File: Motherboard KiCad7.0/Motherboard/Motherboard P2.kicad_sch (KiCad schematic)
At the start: 33 parts, among them J3 2-1445057-2, J4 2-1445057-2, J5 2-1445057-2, J6 2-1445057-2, J7 2-1445057-2, Q1 AO3400A, Q2 AO3400A, Q3 AO3400A, Q4 AO3400A, Q5 AO3400A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

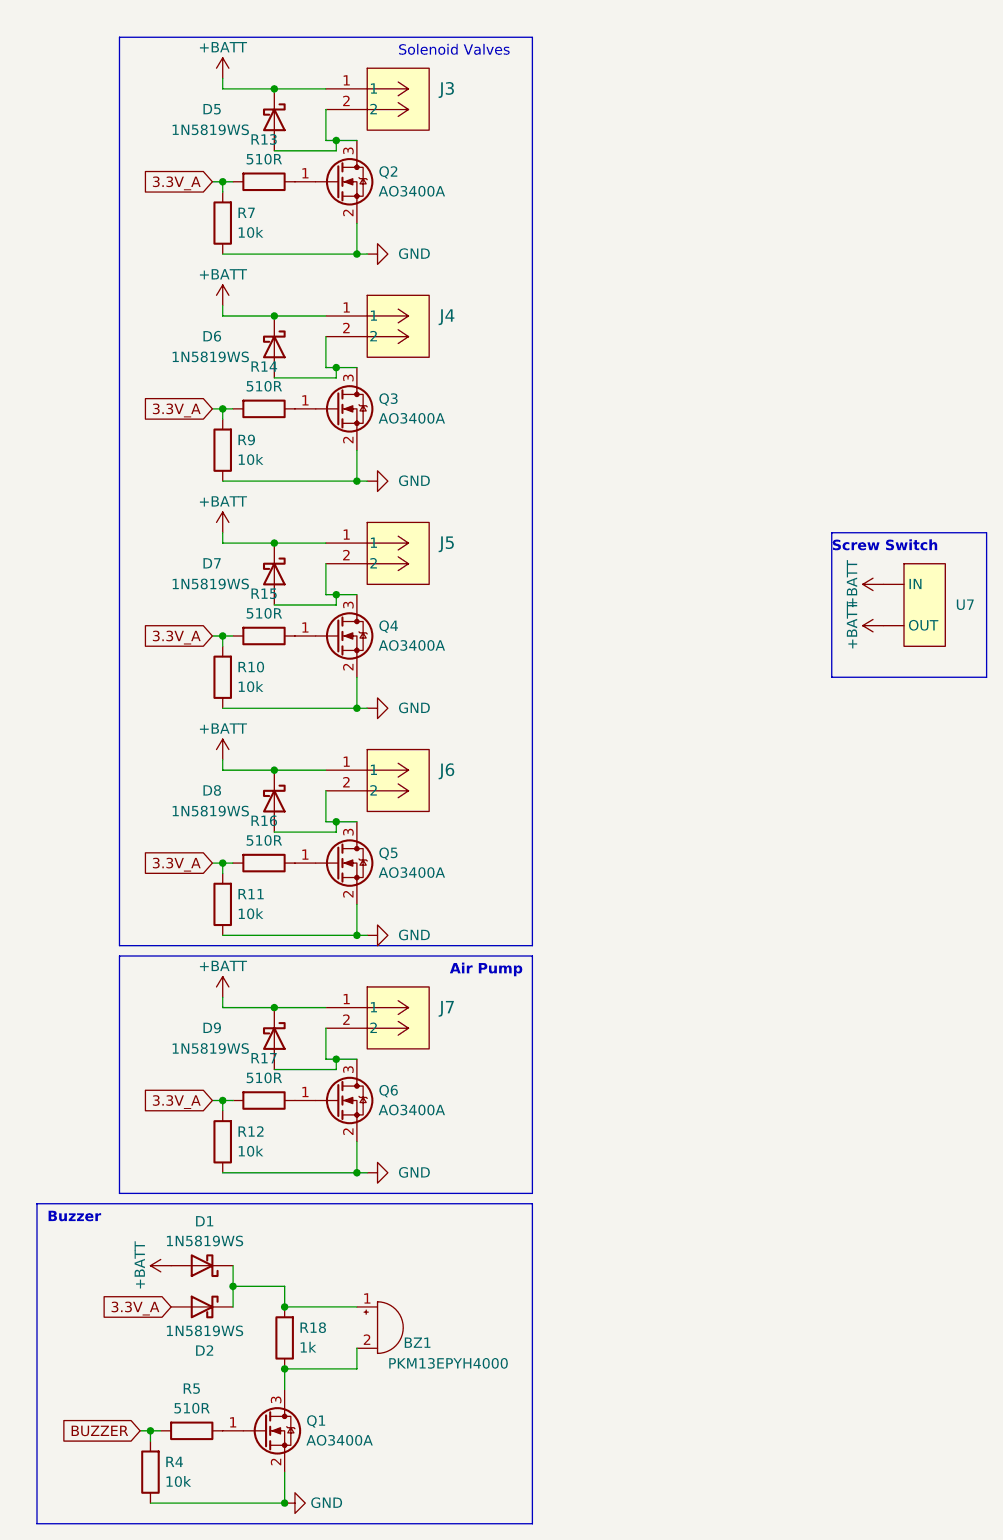
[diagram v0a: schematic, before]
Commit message: Updated screwswitch symbol
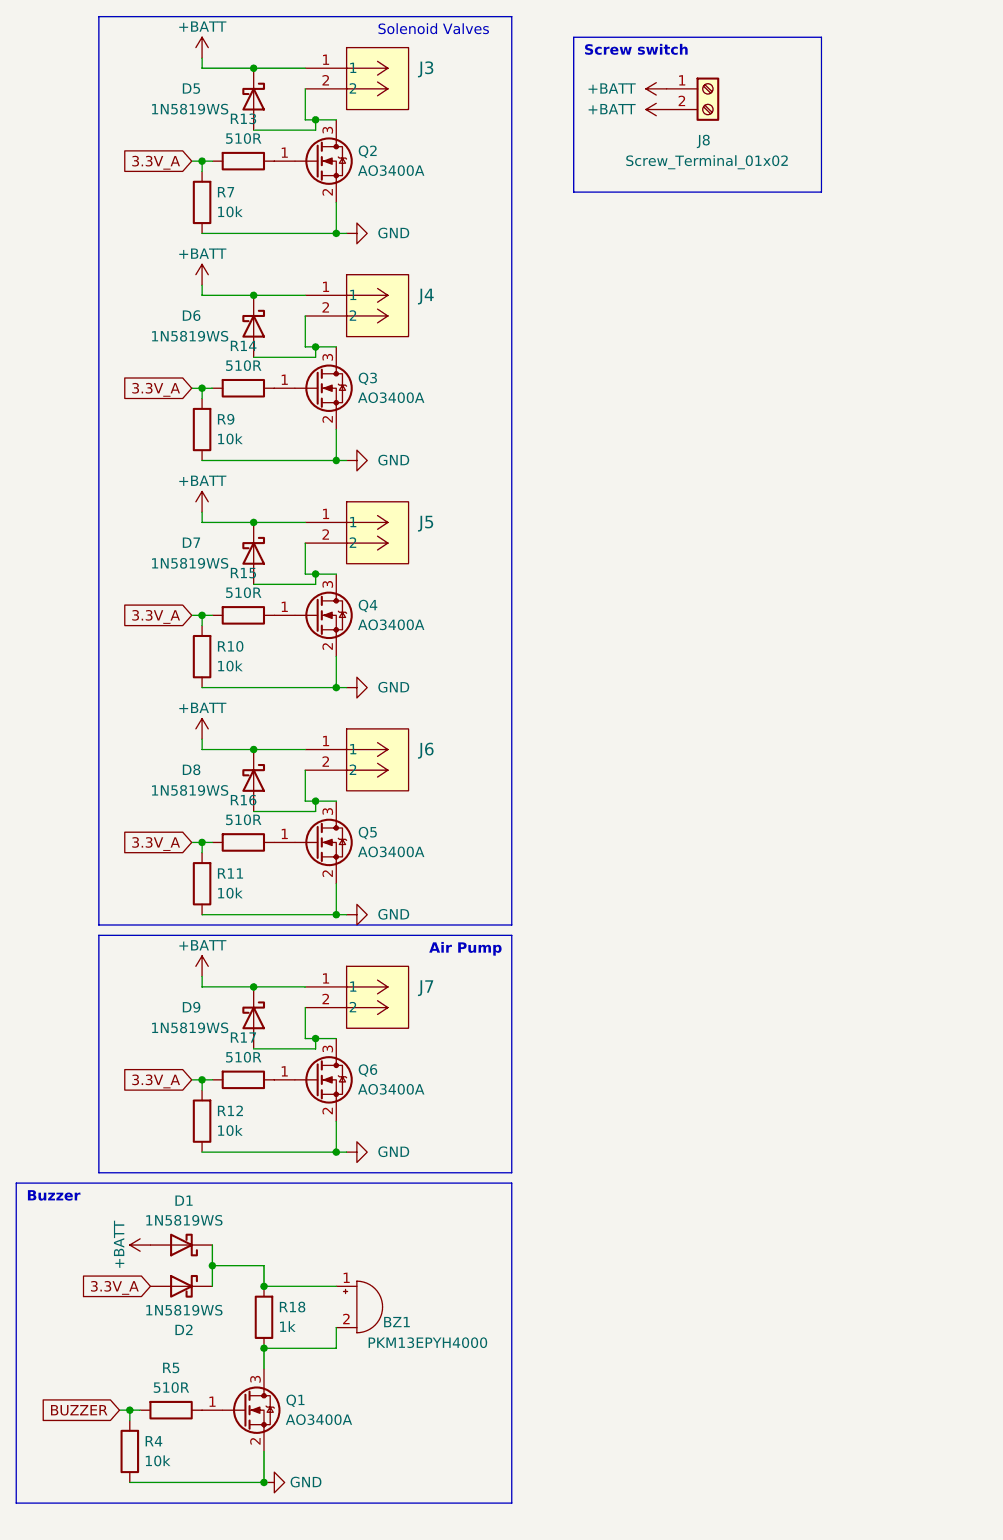
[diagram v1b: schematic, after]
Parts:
- removed U7: ~, symbol Screw Switch:Screw_Switch
- added J8: Screw_Terminal_01x02, symbol Connector:Screw_Terminal_01x02
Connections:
- net +BATT: now also J8.1 (Pin_1), J8.2 (Pin_2)
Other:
- note added: "Screw switch"
- note removed: "Screw Switch"
- moved on the sheet: BZ1, D1, D2, D5, D6, D7, D8, D9, J3, J4, J5, J6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

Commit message: Updated STM32 pinout
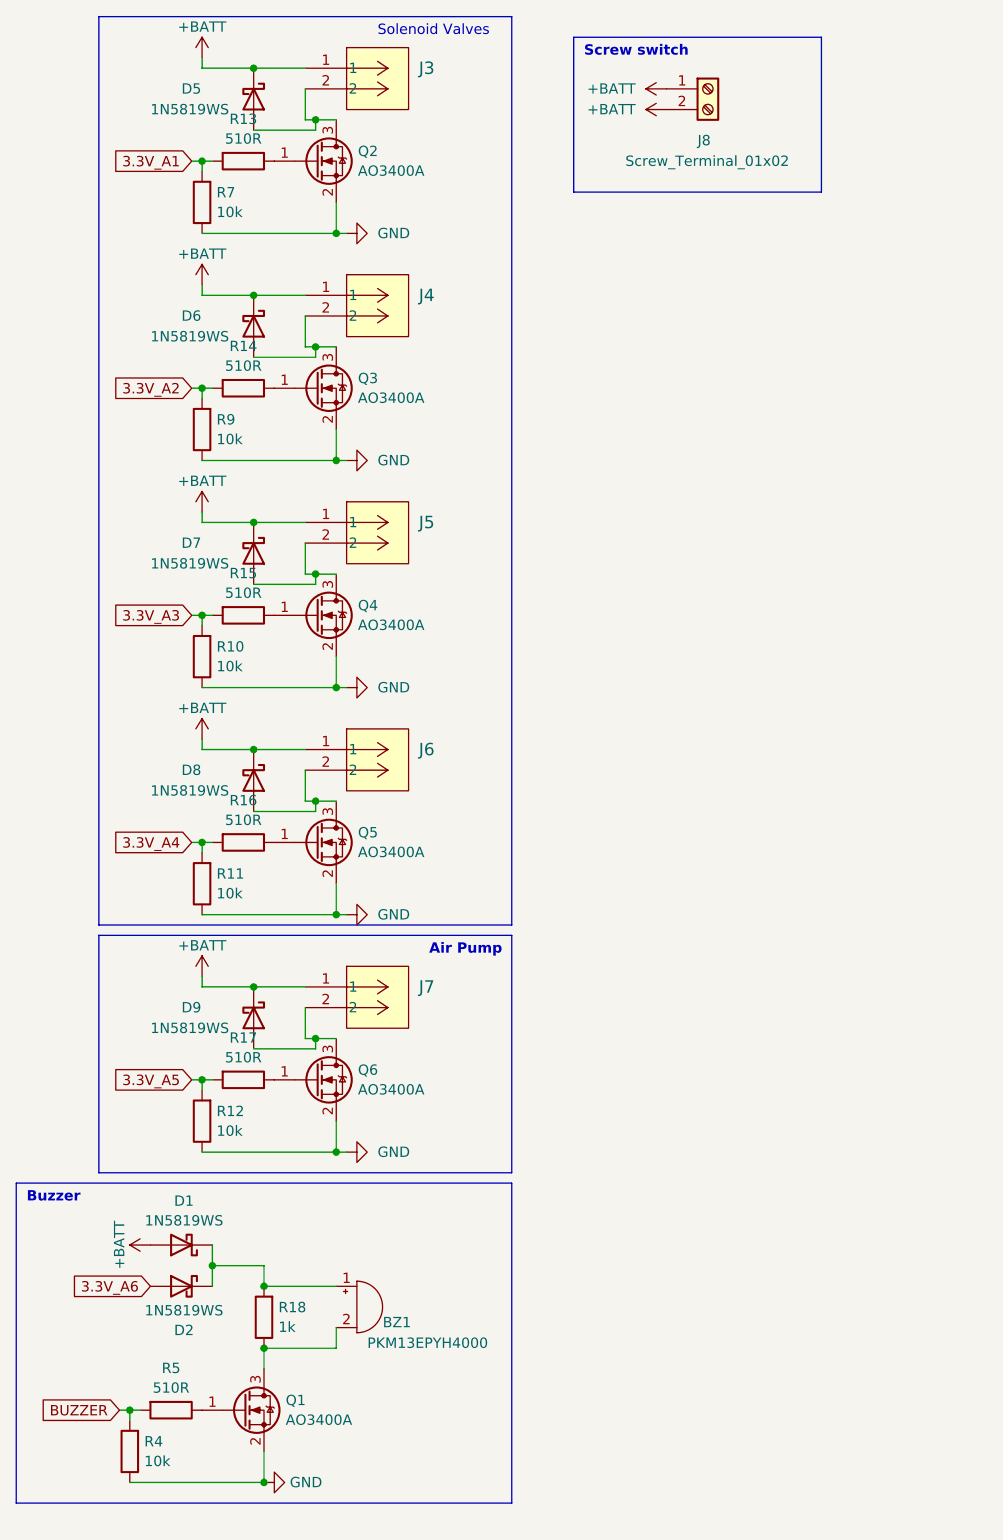
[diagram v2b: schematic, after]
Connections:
- removed net 3.3V_A: D2.2 (A), R10.2, R11.2, R12.2, R13.2, R14.2, R15.2, R16.2, R17.2, R7.2, R9.2
- new net 3.3V_A1: R13.2, R7.2
- new net 3.3V_A2: R14.2, R9.2
- new net 3.3V_A3: R10.2, R15.2
- new net 3.3V_A4: R11.2, R16.2
- new net 3.3V_A5: R12.2, R17.2
- new net 3.3V_A6: D2.2 (A)
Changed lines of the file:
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@@
     (effects (font (size 1.27 1.27) (thickness 0.254) bold) (justify left bottom))
   )
-  (global_label "3.3V_A" (shape input) (at 49.53 87.63 180) (fields_autoplaced)
+  (global_label "3.3V_A3" (shape input) (at 49.53 87.63 180) (fields_autoplaced)
     (effects (font (size 1.27 1.27)) (justify right))
-    (property "Intersheetrefs" "${INTERSHEET_REFS}" (at 40.3762 87.63 0)
+    (property "Intersheetrefs" "${INTERSHEET_REFS}" (at 39.1667 87.63 0)
       (effects (font (size 1.27 1.27)) (justify right) hide)
     )
   )
-  (global_label "3.3V_A" (shape input) (at 49.53 59.69 180) (fields_autoplaced)
+  (global_label "3.3V_A2" (shape input) (at 49.53 59.69 180) (fields_autoplaced)
     (effects (font (size 1.27 1.27)) (justify right))
-    (property "Intersheetrefs" "${INTERSHEET_REFS}" (at 40.3762 59.69 0)
+    (property "Intersheetrefs" "${INTERSHEET_REFS}" (at 39.1667 59.69 0)
       (effects (font (size 1.27 1.27)) (justify right) hide)
     )
   )
-  (global_label "3.3V_A" (shape input) (at 44.45 170.18 180) (fields_autoplaced)
+  (global_label "3.3V_A6" (shape input) (at 44.45 170.18 180) (fields_autoplaced)
     (effects (font (size 1.27 1.27)) (justify right))
-    (property "Intersheetrefs" "${INTERSHEET_REFS}" (at 35.2962 170.18 0)
+    (property "Intersheetrefs" "${INTERSHEET_REFS}" (at 34.0867 170.18 0)
       (effects (font (size 1.27 1.27)) (justify right) hide)
     )
@@
     )
   )
-  (global_label "3.3V_A" (shape input) (at 49.53 31.75 180) (fields_autoplaced)
+  (global_label "3.3V_A1" (shape input) (at 49.53 31.75 180) (fields_autoplaced)
     (effects (font (size 1.27 1.27)) (justify right))
-    (property "Intersheetrefs" "${INTERSHEET_REFS}" (at 40.3762 31.75 0)
+    (property "Intersheetrefs" "${INTERSHEET_REFS}" (at 39.1667 31.75 0)
       (effects (font (size 1.27 1.27)) (justify right) hide)
     )
   )
-  (global_label "3.3V_A" (shape input) (at 49.53 115.57 180) (fields_autoplaced)
+  (global_label "3.3V_A4" (shape input) (at 49.53 115.57 180) (fields_autoplaced)
     (effects (font (size 1.27 1.27)) (justify right))
-    (property "Intersheetrefs" "${INTERSHEET_REFS}" (at 40.3762 115.57 0)
+    (property "Intersheetrefs" "${INTERSHEET_REFS}" (at 39.1667 115.57 0)
       (effects (font (size 1.27 1.27)) (justify right) hide)
     )
   )
-  (global_label "3.3V_A" (shape input) (at 49.53 144.78 180) (fields_autoplaced)
+  (global_label "3.3V_A5" (shape input) (at 49.53 144.78 180) (fields_autoplaced)
     (effects (font (size 1.27 1.27)) (justify right))
-    (property "Intersheetrefs" "${INTERSHEET_REFS}" (at 40.3762 144.78 0)
+    (property "Intersheetrefs" "${INTERSHEET_REFS}" (at 39.1667 144.78 0)
       (effects (font (size 1.27 1.27)) (justify right) hide)
     )

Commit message: Updated power connectors
Updated power connectors. Updated symbols and footprints for all components copied from avionics communications module.
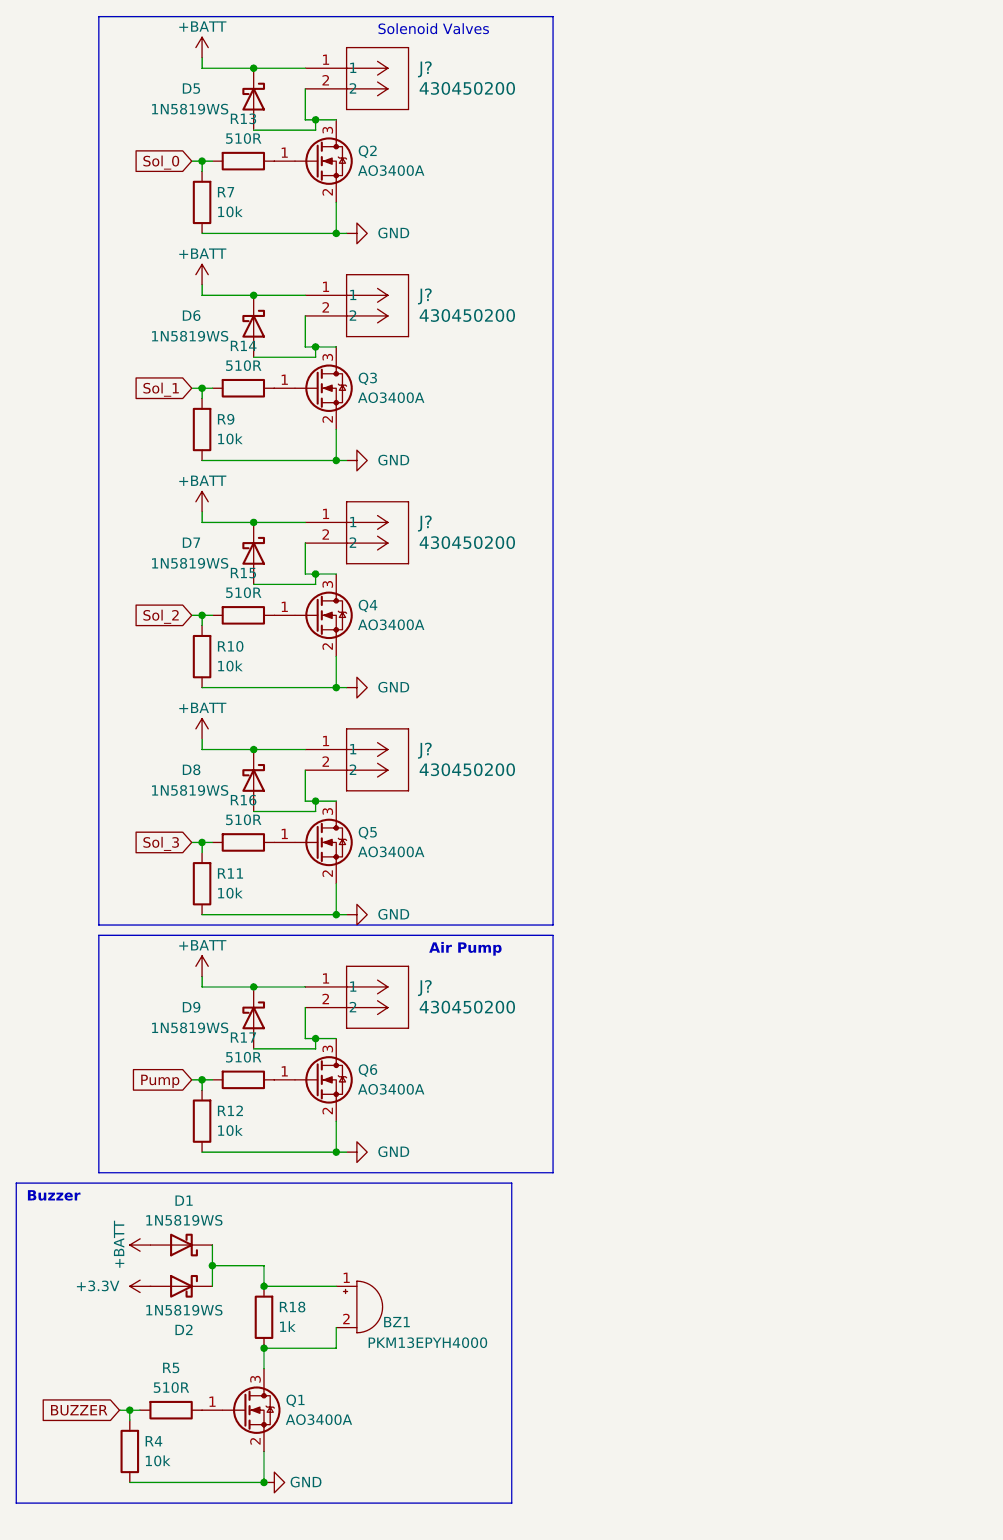
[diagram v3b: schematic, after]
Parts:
- removed J3, J4, J5, J6, J7: 2-1445057-2, CONN_2-1445057-2_TYCO, symbol CONN_2-1445057-2_TYCO:2-1445057-2
- removed J8: Screw_Terminal_01x02, symbol Connector:Screw_Terminal_01x02
- added J? (x5): 430450200, CONN 0430450200:CON_430450200_MOL, symbol CONN 0430450200:430450200
- BZ1: Digikey (none) -> 490-4698-1-ND
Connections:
- net +BATT: now also J?.1, J?.1, J?.1, J?.1, J?.1
- net at D7.2 (A), Q4.3 (D): now also J?.2
- net at D5.2 (A), Q2.3 (D): now also J?.2
- net at D9.2 (A), Q6.3 (D): now also J?.2
- net at D6.2 (A), Q3.3 (D): now also J?.2
- net at D8.2 (A), Q5.3 (D): now also J?.2
- net 3.3V_A1 renamed Sol_0
- net 3.3V_A2 renamed Sol_1
- net 3.3V_A3 renamed Sol_2
- net 3.3V_A4 renamed Sol_3
- net 3.3V_A5 renamed Pump
- net 3.3V_A6 renamed +3.3V
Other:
- note removed: "Screw switch"

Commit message: Updated symbols and fixed circuit
Updated outdated symbols and replaced 3.3V buck converter circuit with a module.
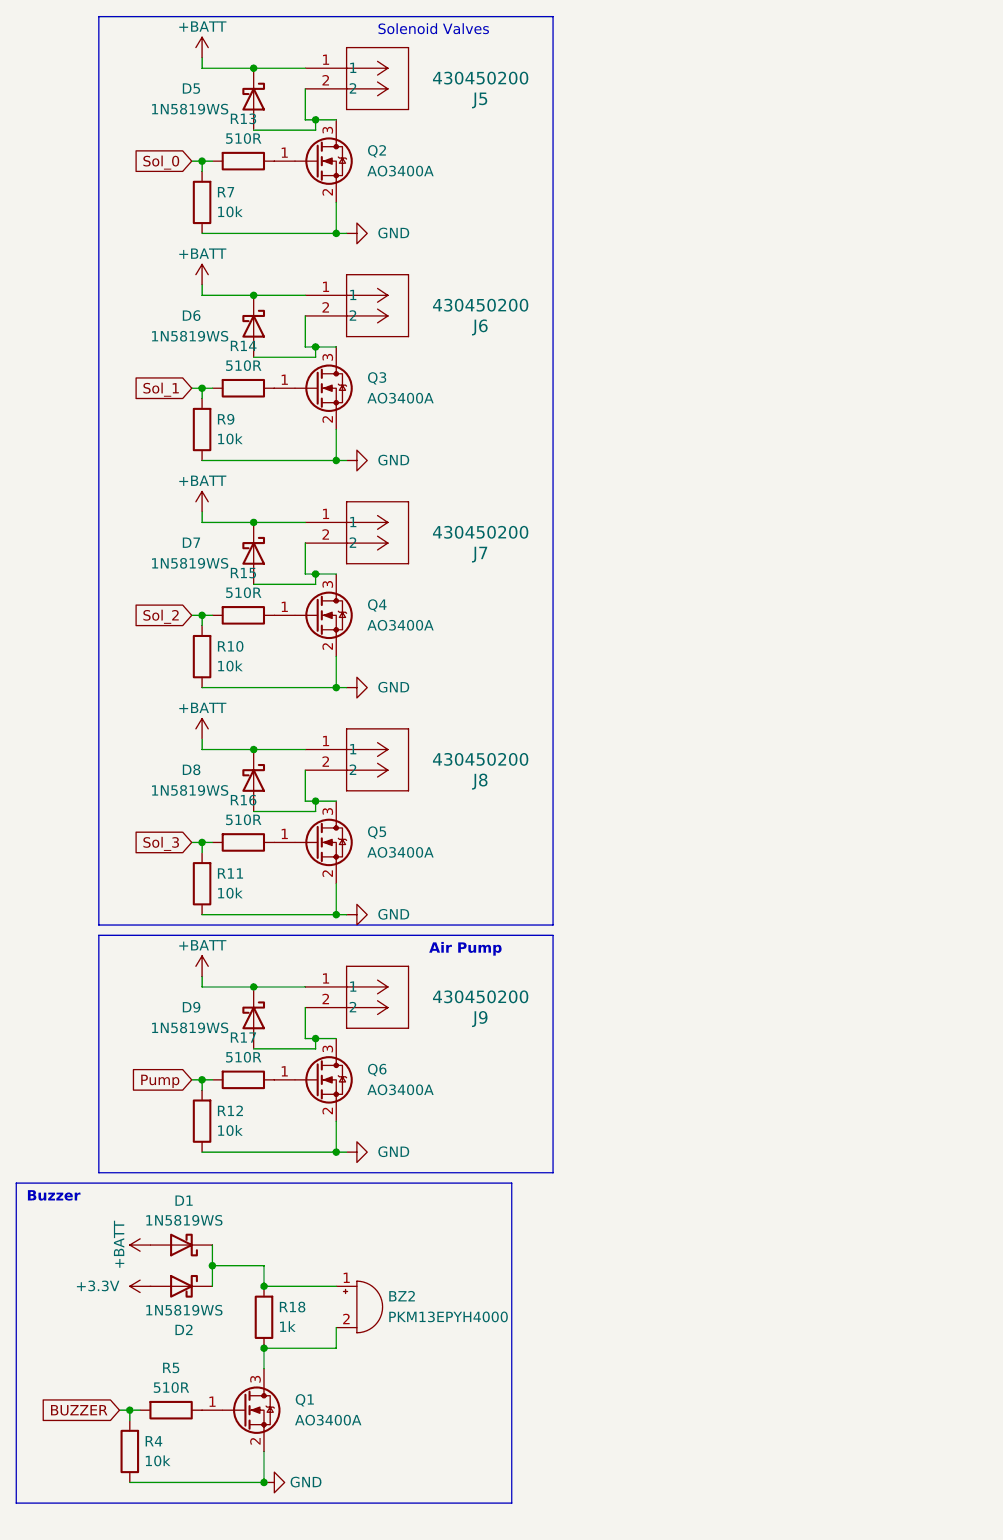
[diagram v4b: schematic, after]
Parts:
- removed BZ1: PKM13EPYH4000, footprints:Buzzer_12.6x9.5RM5.0, symbol Device:Buzzer
- removed J? (x5): 430450200, CONN 0430450200:CON_430450200_MOL, symbol CONN 0430450200:430450200
- added BZ2: PKM13EPYH4000, Buzzer_12.6x9.5RM5.0:Buzzer_12.6x9.5RM5.0, symbol Device:Buzzer
- added J5, J6, J7, J8, J9: 430450200, CON_430450200_MOL, symbol CONN 0430450200:430450200
- Q1, Q2, Q3, Q4, Q5, Q6: LCSC C20917 -> (none)
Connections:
- net +BATT: now also J5.1, J6.1, J7.1, J8.1, J9.1
- net at D5.2 (A), Q2.3 (D): now also J5.2
- net at D7.2 (A), Q4.3 (D): now also J7.2
- net at D8.2 (A), Q5.3 (D): now also J8.2
- net at D1.1 (K), D2.1 (K), R18.2: now also BZ2.1 (+)
- net at D9.2 (A), Q6.3 (D): now also J9.2
- net at D6.2 (A), Q3.3 (D): now also J6.2
- net at Q1.3 (D), R18.1: now also BZ2.2 (-)

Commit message: Added MicroSD reader and part numbers
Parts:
- BZ2: Digikey (none) -> 490-4698-1-ND
- Q1, Q2, Q3, Q4, Q5, Q6: LCSC (none) -> C20917
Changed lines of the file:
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@@
       (effects (font (size 1.27 1.27)) (justify left) hide)
+    )
+    (property "LCSC" "C20917" (at 64.77 59.69 0)
+      (effects (font (size 1.27 1.27)) hide)
     )
     (pin "3")
@@
       (effects (font (size 1.27 1.27)) (justify left) hide)
     )
+    (property "LCSC" "C20917" (at 64.77 115.57 0)
+      (effects (font (size 1.27 1.27)) hide)
+    )
     (pin "3")
     (pin "2")
@@
       (effects (font (size 1.27 1.27)) (justify left) hide)
     )
+    (property "LCSC" "C20917" (at 64.77 144.78 0)
+      (effects (font (size 1.27 1.27)) hide)
+    )
     (pin "3")
     (pin "2")
@@
       (effects (font (size 1.27 1.27)) (justify left) hide)
     )
+    (property "LCSC" "C20917" (at 64.77 31.75 0)
+      (effects (font (size 1.27 1.27)) hide)
+    )
     (pin "3")
     (pin "2")
@@
       (effects (font (size 1.27 1.27)) (justify left) hide)
     )
+    (property "LCSC" "C20917" (at 55.88 185.42 0)
+      (effects (font (size 1.27 1.27)) hide)
+    )
     (pin "3")
     (pin "2")
@@
       (effects (font (size 1.27 1.27)) hide)
     )
+    (property "Digikey" "490-4698-1-ND" (at 69.85 172.72 0)
+      (effects (font (size 1.27 1.27)) hide)
+    )
     (pin "1")
     (pin "2")
@@
       (effects (font (size 1.27 1.27)) (justify left) hide)
     )
+    (property "LCSC" "C20917" (at 64.77 87.63 0)
+      (effects (font (size 1.27 1.27)) hide)
+    )
     (pin "3")
